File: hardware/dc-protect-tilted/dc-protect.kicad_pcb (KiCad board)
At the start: 2 copper layers, 53.6 x 59.9 mm, 5 parts, among them P1 CON-SENSOR2-BLANK, U1 DC-Protect

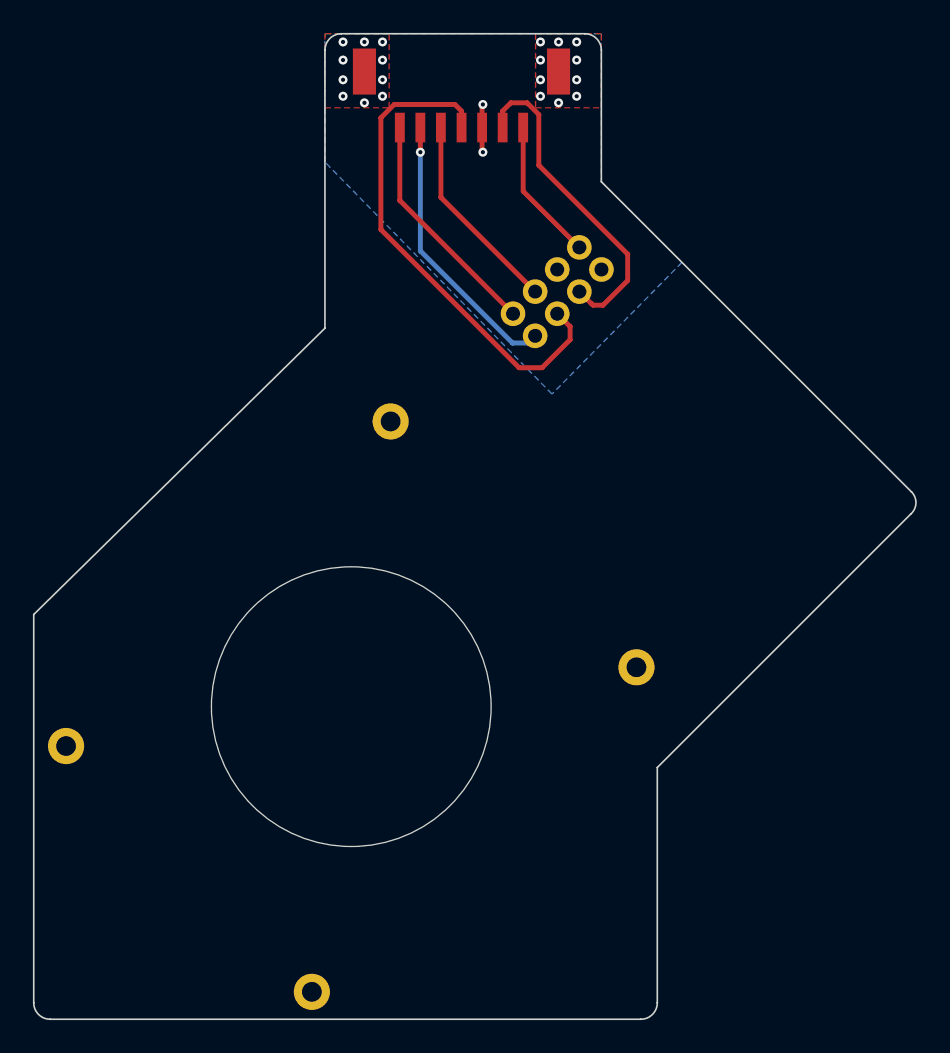
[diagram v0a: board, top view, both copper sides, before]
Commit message: add version 1.2
 * change dc protect drill diameter (20mm)
 * cut lower PCB corners
 * increase 7pole mount pad size
 * increase version number
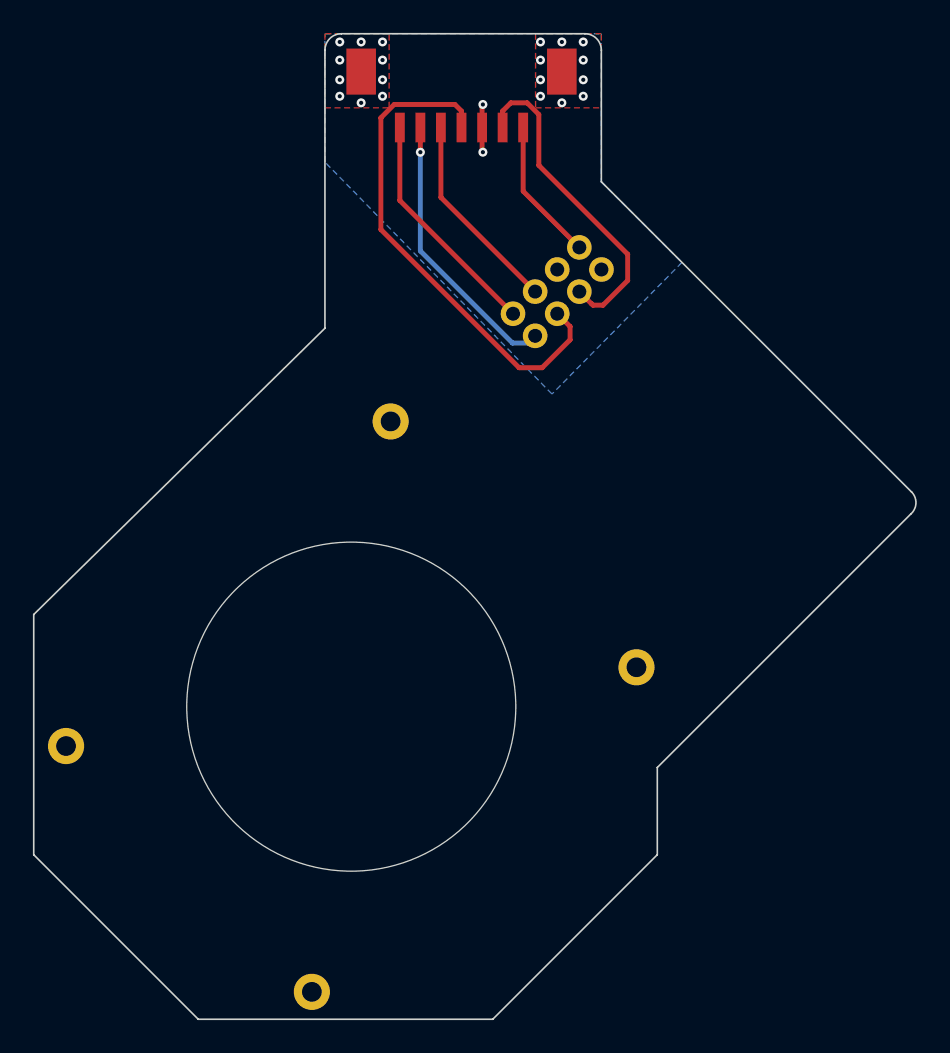
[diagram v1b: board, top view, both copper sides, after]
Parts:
- moved VAL 7.63 mm to (188.8, 106.4)
- moved G*** 6.34 mm to (201.4, 105.1)
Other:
- outline, holes or cut-outs redrawn
- board text added: "DC-Protect 1.2"
- board text removed: "DC-Protect 1.1"
